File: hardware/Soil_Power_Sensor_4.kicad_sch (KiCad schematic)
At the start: 19 parts, among them J3 Debug, J5 Micro_SD_Card, Q2 L8050QLT1G, Q3 L8050QLT1G, SW1 BOOT, SW2 EN, U8 ESP32-C3-WROOM-02-N4

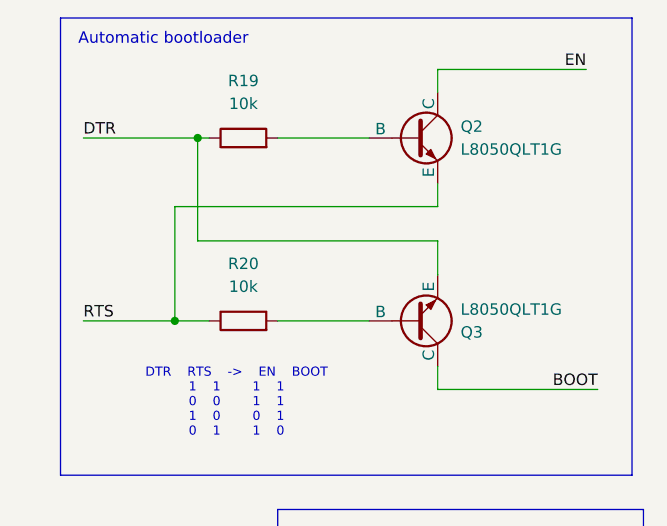
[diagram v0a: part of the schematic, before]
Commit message: Fixed issues from design review
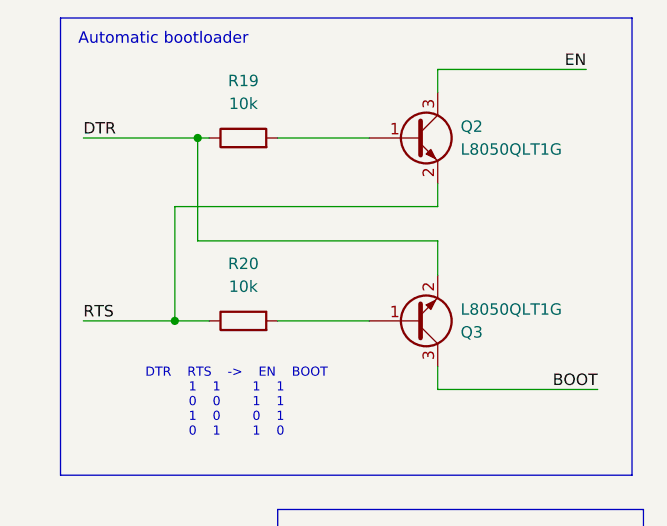
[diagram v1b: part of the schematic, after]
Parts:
- Q2, Q3: symbol Simulation_SPICE:NPN -> Device:Q_NPN_BEC
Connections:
- net BOOT: now also Q3.3 (C); no longer Q3.1 (C)
- net DTR: now also Q3.2 (E); no longer Q3.3 (E)
- net EN: now also Q2.3 (C); no longer Q2.1 (C)
- net RTS: now also Q2.2 (E); no longer Q2.3 (E)
- net at R19.2: now also Q2.1 (B); no longer Q2.2 (B)
- net at R20.2: now also Q3.1 (B); no longer Q3.2 (B)
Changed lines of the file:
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@@
 	)
 	(symbol
-		(lib_id "Simulation_SPICE:NPN")
+		(lib_id "Device:Q_NPN_BEC")
 		(at 252.73 50.8 0)
 		(mirror x)
@@
 		)
 		(property "Footprint" "Package_TO_SOT_SMD:SOT-23"
-			(at 316.23 50.8 0)
-			(effects
-				(font
-					(size 1.27 1.27)
-				)
-				(hide yes)
-			)
-		)
-		(property "Datasheet" "https://ngspice.sourceforge.io/docs/ngspice-html-manual/manual.xhtml#cha_BJTs"
-			(at 316.23 50.8 0)
-			(effects
-				(font
-					(size 1.27 1.27)
-				)
-				(hide yes)
-			)
-		)
-		(property "Description" "Bipolar transistor symbol for simulation only, substrate tied to the emitter"
+			(at 257.81 53.34 0)
+			(effects
+				(font
+					(size 1.27 1.27)
+				)
+				(hide yes)
+			)
+		)
+		(property "Datasheet" "~"
+			(at 252.73 50.8 0)
+			(effects
+				(font
+					(size 1.27 1.27)
+				)
+				(hide yes)
+			)
+		)
+		(property "Description" "NPN transistor, base/emitter/collector"
 			(at 252.73 50.8 0)
 			(effects
@@
 	)
 	(symbol
-		(lib_id "Simulation_SPICE:NPN")
+		(lib_id "Device:Q_NPN_BEC")
 		(at 252.73 30.48 0)
 		(unit 1)
@@
 		)
 		(property "Footprint" "Package_TO_SOT_SMD:SOT-23"
-			(at 316.23 30.48 0)
-			(effects
-				(font
-					(size 1.27 1.27)
-				)
-				(hide yes)
-			)
-		)
-		(property "Datasheet" "https://ngspice.sourceforge.io/docs/ngspice-html-manual/manual.xhtml#cha_BJTs"
-			(at 316.23 30.48 0)
-			(effects
-				(font
-					(size 1.27 1.27)
-				)
-				(hide yes)
-			)
-		)
-		(property "Description" "Bipolar transistor symbol for simulation only, substrate tied to the emitter"
+			(at 257.81 27.94 0)
+			(effects
+				(font
+					(size 1.27 1.27)
+				)
+				(hide yes)
+			)
+		)
+		(property "Datasheet" "~"
 			(at 252.73 30.48 0)
 			(effects
+				(font
+					(size 1.27 1.27)
+				)
+				(hide yes)
+			)
+		)
+		(property "Description" "NPN transistor, base/emitter/collector"
+			(at 252.73 30.48 0)
+			(effects

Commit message: usb ttl components
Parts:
- added J16: USB_C_Receptacle_USB2.0_16P, Connector_USB:USB_C_Receptacle_GCT_USB4110, symbol Connector:USB_C_Receptacle_USB2.0_16P
- added R30, R31: 0, Resistor_SMD:R_0603_1608Metric, symbol Device:R
- added R32, R33: 5.1k, Resistor_SMD:R_0603_1608Metric, symbol Device:R
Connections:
- net GND: now also J16.A1 (GND), J16.A12 (GND), J16.B1 (GND), J16.B12 (GND), J16.S1 (SHIELD), R32.2, R33.2
- net USB_D+: now also J16.A7 (D-), J16.B7 (D-), R31.2; no longer U8.14 (IO19)
- net USB_D-: now also J16.A6 (D+), J16.B6 (D+), R30.2; no longer U8.13 (IO18)
- new net: R30.1, U8.13 (IO18)
- new net: R31.1, U8.14 (IO19)
- new net: J16.B5 (CC2), R33.1
- new net: J16.A4 (VBUS), J16.A9 (VBUS), J16.B4 (VBUS), J16.B9 (VBUS)
- new net: J16.A5 (CC1), R32.1
- no-connect marks 0 -> 3
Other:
- note added: "Full USB PHY inside ESP32"
- note added: "USB CDC"
- moved on the sheet: C12, C13, C16, J3, JP5, Q2, Q3, R15, R19, R20, SW1, SW2

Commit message: john pcb review feedback
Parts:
- removed J16: USB_C_Receptacle_USB2.0_16P, Connector_USB:USB_C_Receptacle_GCT_USB4110, symbol Connector:USB_C_Receptacle_USB2.0_16P
- removed J3: Debug, Connector_PinHeader_2.54mm:PinHeader_2x05_P2.54mm_Vertical, symbol Connector_Generic:Conn_02x05_Odd_Even
- removed JP5: ESP_EN, Jumper:SolderJumper-3_P1.3mm_Open_Pad1.0x1.5mm, symbol Jumper:SolderJumper_3_Bridged12
- removed Q2, Q3: L8050QLT1G, Package_TO_SOT_SMD:SOT-23, symbol Device:Q_NPN_BEC
- removed R19, R20: 10k, Resistor_SMD:R_0603_1608Metric, symbol Device:R
- removed R32, R33: 5.1k, Resistor_SMD:R_0603_1608Metric, symbol Device:R
- added J15: Conn_01x02, symbol Connector:Conn_01x03_Pin
- renumbered C12 to C17, C13 to C18, J5 to J16, R14 to R27, R12 to R28, R30 to R29, R31 to R30, R15 to R31, SW1 to SW5, SW2 to SW6, U8 to U9
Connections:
- net ESP32_EN: now also R31.1
- net GND: now also J15.3 (Pin_3)
- net USB_D+: now also J15.2 (Pin_2)
- net USB_D-: now also J15.1 (Pin_1)
- no-connect marks 3 -> 0
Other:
- note added: "serial over usb cdc"
- note removed: "Automatic bootloader"
- note removed: "DTR RTS -> EN BOOT 1 1 1 1 0 0 1 1 1 0 0 1 0 1 1 0"
- note removed: "Debug header"
- note removed: "Full USB PHY inside ESP32"
- note removed: "USB CDC"

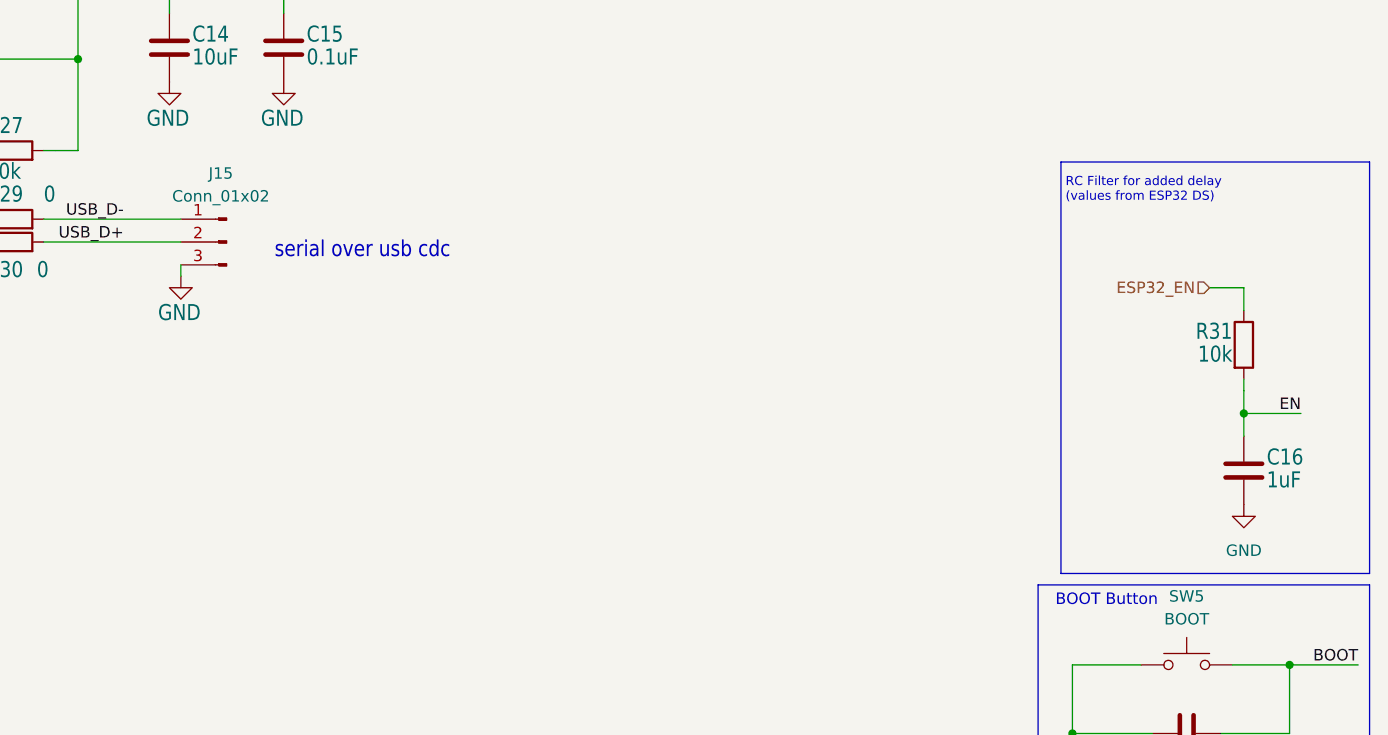
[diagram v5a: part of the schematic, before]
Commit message: pcb outline
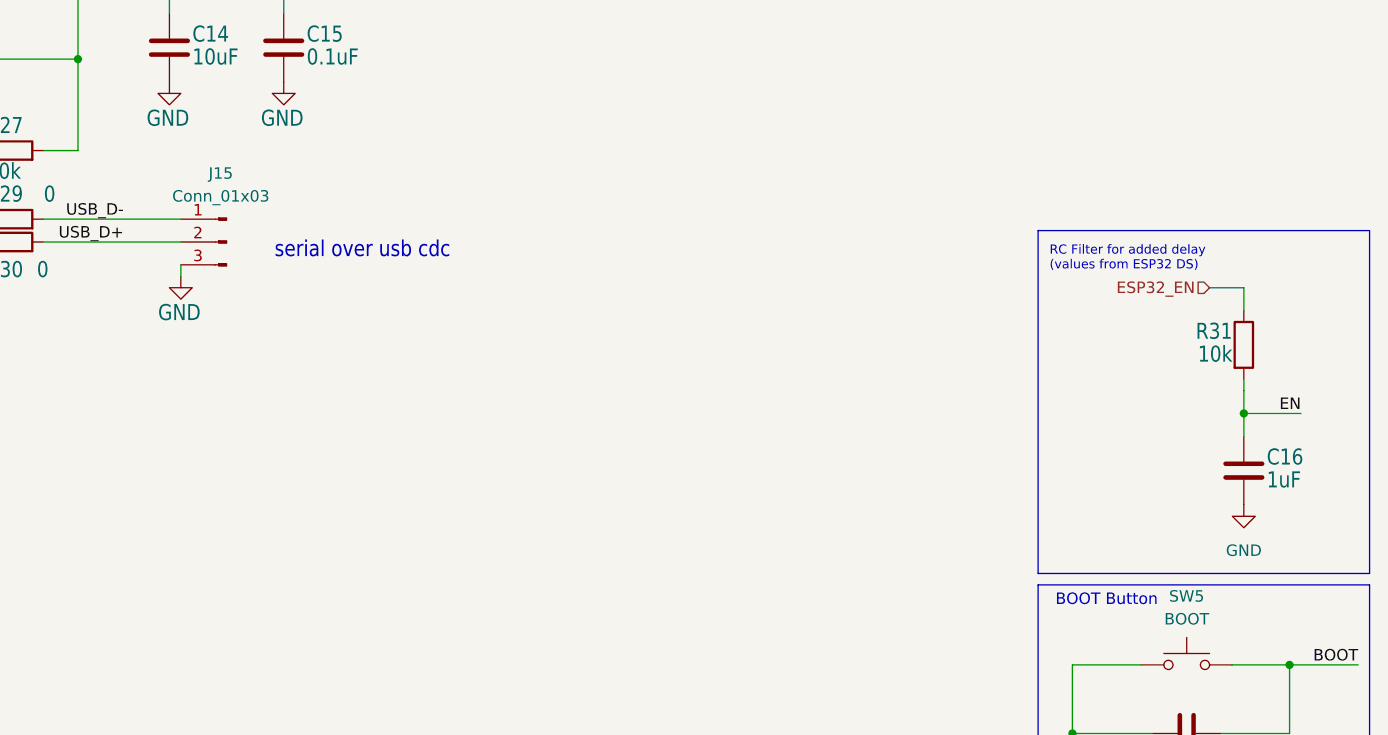
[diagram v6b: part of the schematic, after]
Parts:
- J15: value Conn_01x02 -> Conn_01x03; footprint (none) -> Connector_PinHeader_2.54mm:PinHeader_1x03_P2.54mm_Vertical
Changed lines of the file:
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@@
 	)
 	(rectangle
-		(start 250.19 63.5)
+		(start 247.65 71.12)
 		(end 284.48 109.22)
 		(stroke
@@
 	(text "RC Filter for added delay\n(values from ESP32 DS)"
 		(exclude_from_sim no)
-		(at 250.698 68.072 0)
+		(at 248.92 75.692 0)
 		(effects
 			(font
@@
 			)
 		)
-		(property "Value" "Conn_01x02"
+		(property "Value" "Conn_01x03"
 			(at 156.845 67.31 0)
 			(effects
@@
 			)
 		)
-		(property "Footprint" ""
+		(property "Footprint" "Connector_PinHeader_2.54mm:PinHeader_1x03_P2.54mm_Vertical"
 			(at 157.48 72.39 0)
 			(effects

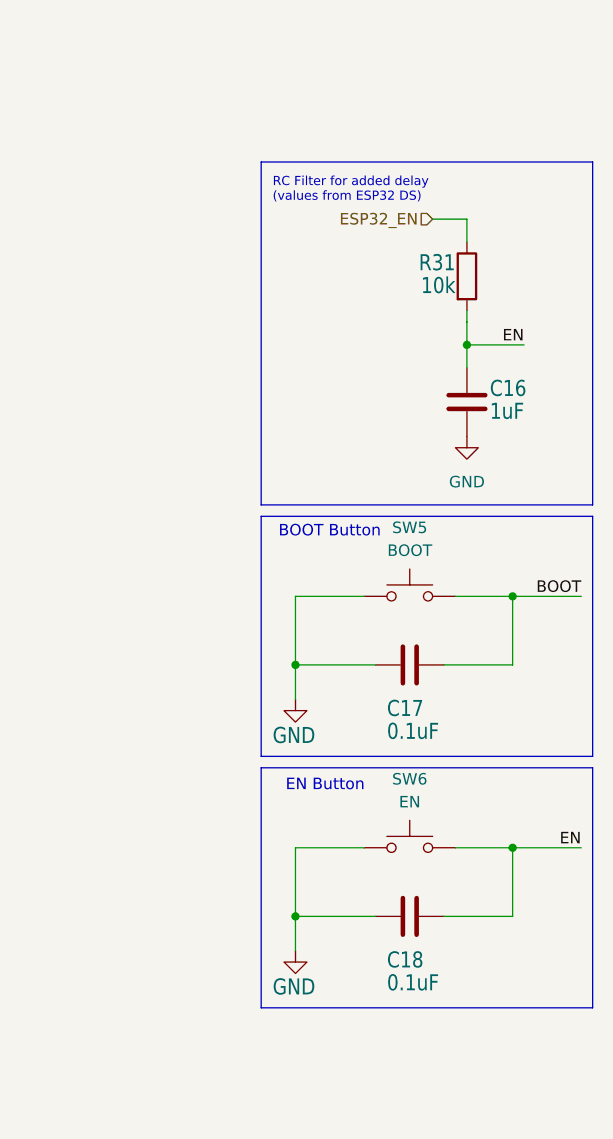
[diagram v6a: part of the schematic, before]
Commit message: pin numbering and changed mosfets
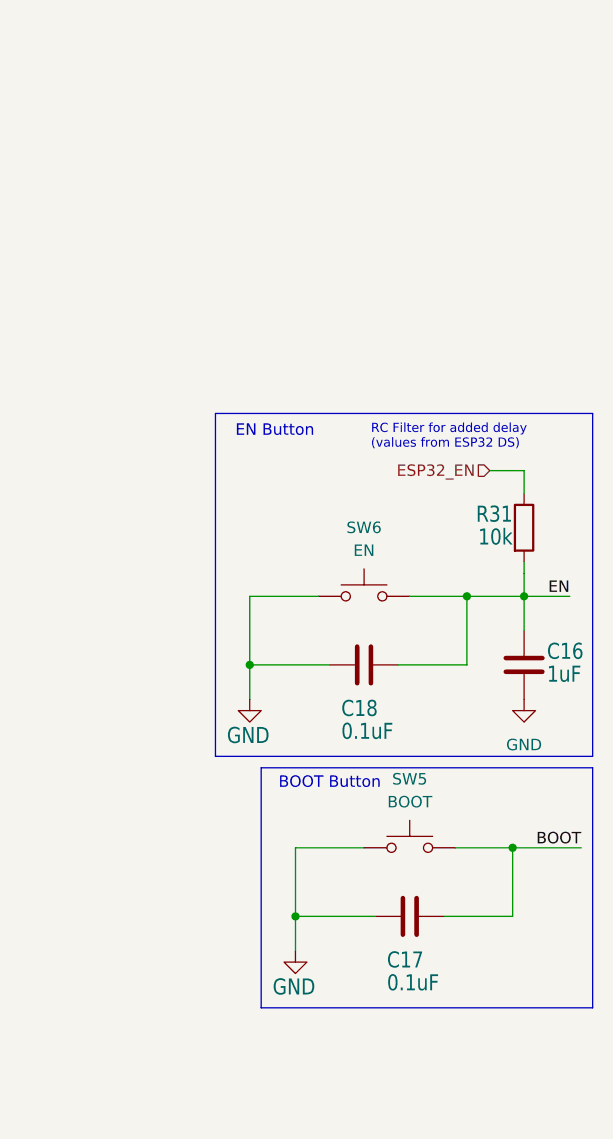
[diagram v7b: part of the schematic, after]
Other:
- moved on the sheet: C16, C17, C18, R31, SW5, SW6

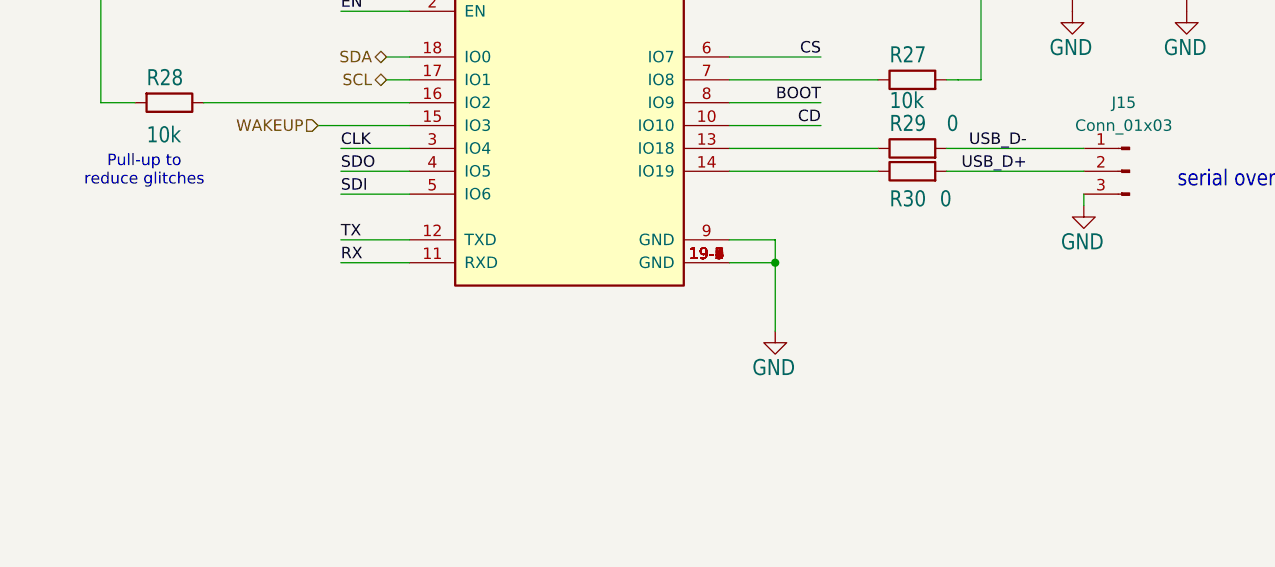
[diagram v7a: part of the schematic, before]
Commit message: lower power buck-boost
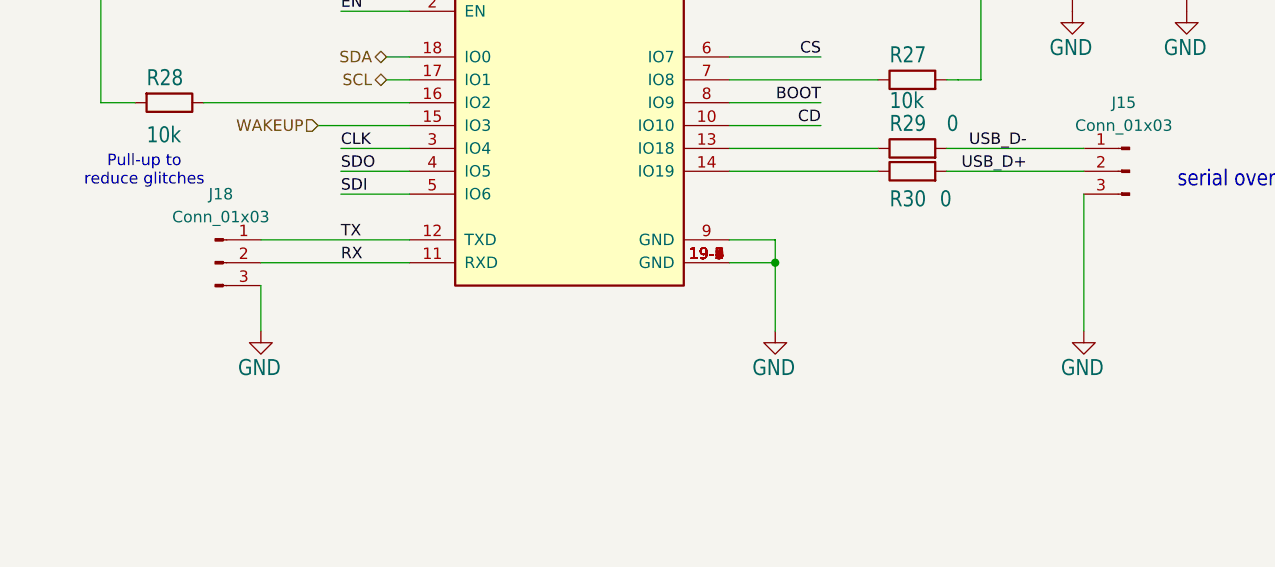
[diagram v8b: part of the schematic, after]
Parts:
- added J18: Conn_01x03, Connector_PinHeader_2.54mm:PinHeader_1x03_P2.54mm_Vertical, symbol Connector:Conn_01x03_Pin
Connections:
- net GND: now also J18.3 (Pin_3)
- net RX: now also J18.2 (Pin_2)
- net TX: now also J18.1 (Pin_1)
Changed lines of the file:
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@@
 	(wire
 		(pts
-			(xy 69.85 80.01) (xy 77.47 80.01)
+			(xy 60.96 80.01) (xy 77.47 80.01)
 		)
 		(stroke
@@
 	(wire
 		(pts
+			(xy 60.96 90.17) (xy 60.96 85.09)
+		)
+		(stroke
+			(width 0)
+			(type default)
+		)
+	)
+	(wire
+		(pts
 			(xy 246.38 127) (xy 246.38 130.81)
 		)
@@
 	(wire
 		(pts
-			(xy 152.4 76.2) (xy 152.4 74.93)
+			(xy 152.4 90.17) (xy 152.4 74.93)
 		)
 		(stroke
@@
 	(wire
 		(pts
-			(xy 69.85 82.55) (xy 77.47 82.55)
+			(xy 60.96 82.55) (xy 77.47 82.55)
 		)
 		(stroke
@@
 	(symbol
 		(lib_id "power:GND")
+		(at 60.96 90.17 0)
+		(unit 1)
+		(exclude_from_sim no)
+		(in_bom yes)
+		(on_board yes)
+		(dnp no)
+		(property "Reference" "#GND017"
+			(at 60.96 90.17 0)
+			(effects
+				(font
+					(size 1.27 1.27)
+				)
+				(hide yes)
+			)
+		)
+		(property "Value" "GND"
+			(at 58.42 95.25 0)
+			(effects
+				(font
+					(size 1.778 1.5113)
+				)
+				(justify left bottom)
+			)
+		)
+		(property "Footprint" ""
+			(at 60.96 90.17 0)
+			(effects
+				(font
+					(size 1.27 1.27)
+				)
+				(hide yes)
+			)
+		)
+		(property "Datasheet" ""
+			(at 60.96 90.17 0)
+			(effects
+				(font
+					(size 1.27 1.27)
+				)
+				(hide yes)
+			)
+		)
+		(property "Description" "Power symbol creates a global label with name \"GND\" , ground"
+			(at 60.96 90.17 0)
+			(effects
+				(font
+					(size 1.27 1.27)
+				)
+				(hide yes)
+			)
+		)
+		(pin "1"
+		)
+		(instances
+			(project "Soil Power Sensor"
+				(path "/5300ec4d-4648-40a1-8d89-4fa6b3bf32a3/1383843a-880b-4efd-8c7f-ecdf3639f794"
+					(reference "#GND017")
+					(unit 1)
+				)
+			)
+		)
+	)
+	(symbol
+		(lib_id "power:GND")
 		(at 276.86 130.81 0)
 		(unit 1)
@@
 	(symbol
 		(lib_id "power:GND")
-		(at 152.4 76.2 0)
+		(at 152.4 90.17 0)
 		(unit 1)
 		(exclude_from_sim no)
@@
 		(dnp no)
 		(property "Reference" "#GND016"
-			(at 152.4 76.2 0)
+			(at 152.4 90.17 0)
 			(effects
 				(font
@@
 		)
 		(property "Value" "GND"
-			(at 149.86 81.28 0)
+			(at 149.86 95.25 0)
 			(effects
 				(font
@@
 		)
 		(property "Footprint" ""
-			(at 152.4 76.2 0)
+			(at 152.4 90.17 0)
 			(effects
 				(font
@@
 		)
 		(property "Datasheet" ""
-			(at 152.4 76.2 0)
+			(at 152.4 90.17 0)
 			(effects
 				(font
@@
 		)
 		(property "Description" "Power symbol creates a global label with name \"GND\" , ground"
-			(at 152.4 76.2 0)
+			(at 152.4 90.17 0)
 			(effects
 				(font
@@
 					(unit 1)
 				)
+			)
+		)
+	)
+	(symbol
+		(lib_id "Connector:Conn_01x03_Pin")
+		(at 55.88 82.55 0)
+		(unit 1)
+		(exclude_from_sim no)
+		(in_bom yes)
+		(on_board yes)
+		(dnp no)
+		(property "Reference" "J18"
+			(at 56.515 74.93 0)
+			(effects
+				(font
+					(size 1.27 1.27)
+				)
+			)
+		)
+		(property "Value" "Conn_01x03"
+			(at 56.515 77.47 0)
+			(effects
+				(font
+					(size 1.27 1.27)
+				)
+			)
+		)
+		(property "Footprint" "Connector_PinHeader_2.54mm:PinHeader_1x03_P2.54mm_Vertical"
+			(at 55.88 82.55 0)
+			(effects
+				(font
+					(size 1.27 1.27)
+				)
+				(hide yes)
+			)
+		)
+		(property "Datasheet" "~"
+			(at 55.88 82.55 0)
+			(effects
+				(font
+					(size 1.27 1.27)
+				)
+				(hide yes)
+			)
+		)
+		(property "Description" "Generic connector, single row, 01x03, script generated"
+			(at 55.88 82.55 0)
+			(effects
+				(font
+					(size 1.27 1.27)
+				)
+				(hide yes)
+			)
+		)
+		(pin "1"
+		)
+		(pin "2"
+		)
+		(pin "3"
+		)
+		(instances
+			(project "Soil Power Sensor"
+				(path "/5300ec4d-4648-40a1-8d89-4fa6b3bf32a3/1383843a-880b-4efd-8c7f-ecdf3639f794"
+					(reference "J18")
+					(unit 1)
+				)
